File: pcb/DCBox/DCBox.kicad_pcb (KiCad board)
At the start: 2 copper layers, 60 x 50 mm, 7 parts, among them J1 DC-IN, J2 Out-1, J3 Out-2, J4 Out-3

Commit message: 1. 完善布局
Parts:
- added C1: NC, lc_lib:0603_R, F.Cu at (163.9, 64.1)
- added C10: 1uF, lc_lib:0603_R, F.Cu at (150.3, 63.9)
- added C11: NC, lc_lib:0603_R, F.Cu at (169.8, 54.7)
- added C12: NC, lc_lib:0603_R, F.Cu at (173.3, 49.2)
- added C13: NC, lc_lib:0603_R, F.Cu at (177.6, 46.4)
- added C14: 22uF, lc_lib:1206_R, F.Cu at (164.0, 46.8)
- added C15: 100nF, lc_lib:0603_R, F.Cu at (155.7, 69.9)
- added C16: 100nF, lc_lib:0603_R, F.Cu at (155.4, 61.5)
- added C17: 22uF, lc_lib:1206_R, F.Cu at (157.8, 52.6)
- added C18: 100nF, lc_lib:0603_R, F.Cu at (159.6, 61.5)
- added C19: 22uF, lc_lib:1206_R, F.Cu at (156.2, 58.3)
- added C2: NC, lc_lib:0603_R, F.Cu at (155.7, 67.1)
- added C20: 100nF, lc_lib:0603_R, F.Cu at (163.9, 61.3)
- added C21: NC, lc_lib:0603_R, F.Cu at (143.3, 79.7)
- added C22: NC, lc_lib:0603_R, F.Cu at (169.1, 49.2)
- added C3: NC, lc_lib:0603_R, F.Cu at (155.7, 72.6)
- added C4: 4.7uF, lc_lib:0603_R, F.Cu at (151.5, 72.3)
- added C5: 100nF, lc_lib:0603_R, F.Cu at (139.1, 80.4)
- added C6: 4.7uF, lc_lib:0603_R, F.Cu at (142.9, 74.2)
- added C7: 100nF, lc_lib:0603_R, F.Cu at (151.5, 69.5)
- added C8: 2.2uF, lc_lib:0603_R, F.Cu at (169.1, 46.4)
- added C9: 1uF, lc_lib:0603_R, F.Cu at (134.8, 80.4)
- added D1: LED, lc_lib:0603_LED_N1, F.Cu at (151.4, 49.4)
- added D2: LED, lc_lib:0603_LED_N1, F.Cu at (151.4, 46.5)
- added D3: LED, lc_lib:0603_LED_N1, F.Cu at (157.6, 49.4)
- added D4: LED, lc_lib:0603_LED_N1, F.Cu at (151.4, 55.1)
- added D5: LED, lc_lib:0603_LED_N1, F.Cu at (151.4, 52.3)
- added D6: LED, lc_lib:0603_LED_N1, F.Cu at (144.8, 64.0)
- added D7: LED, lc_lib:0603_LED_N1, F.Cu at (157.6, 46.5)
- added J5: Out-4, jld:DC005, F.Cu at (162.3, 151.1)
- added J6: USB_A, Connector_USB:USB_A_Wuerth_614004134726_Horizontal, F.Cu at (158.7, 117.7)
- added J7: USB_A, Connector_USB:USB_A_Wuerth_614004134726_Horizontal, F.Cu at (158.7, 128.7)
- added J8: Conn_01x04, Connector_PinHeader_2.54mm:PinHeader_1x04_P2.54mm_Vertical, F.Cu at (146.3, 47.3)
- added R10: 560k, lc_lib:0603_R, F.Cu at (147.2, 71.4)
- added R11: 1R/2W/%1, lc_lib:2512_R, B.Cu at (162.3, 147.4)
- added R12: 1k, lc_lib:0603_R, F.Cu at (165.5, 57.5)
- added R13: 20k, lc_lib:0603_R, F.Cu at (169.8, 57.5)
- added R14: 10k, lc_lib:0603_R, F.Cu at (134.8, 77.7)
- added R15: 1R/2W/%1, lc_lib:2512_R, B.Cu at (166.9, 117.7)
- added R16: 1R/2W/%1, lc_lib:2512_R, B.Cu at (166.7, 128.5)
- added R17: 15k, lc_lib:0603_R, F.Cu at (154.6, 64.3)
- added R18: 20k, lc_lib:0603_R, F.Cu at (168.2, 60.3)
- added R19: 4.7k, lc_lib:0603_R, F.Cu at (147.6, 79.7)
- added R20: 4.7k, lc_lib:0603_R, F.Cu at (139.1, 77.7)
- added R21: 1k, lc_lib:0603_R, F.Cu at (161.3, 58.5)
- added R22: 1k, lc_lib:0603_R, F.Cu at (147.6, 76.9)
- added R23: 1k, lc_lib:0603_R, F.Cu at (168.4, 52.0)
- added R24: 1k, lc_lib:0603_R, F.Cu at (143.3, 76.9)
- added R25: 1k, lc_lib:0603_R, F.Cu at (174.1, 54.7)
- added R26: 1k, lc_lib:0603_R, F.Cu at (149.2, 66.8)
- added R27: 10k, lc_lib:0603_R, F.Cu at (165.5, 54.7)
- added R28: 1k, lc_lib:0603_R, F.Cu at (151.9, 75.4)
- added R29: 1k, lc_lib:0603_R, F.Cu at (158.9, 64.3)
- added R30: 1.5k, lc_lib:0603_R, F.Cu at (172.7, 52.0)
- added R4: 1k, lc_lib:0603_R, F.Cu at (147.2, 74.2)
- added R5: 1k, lc_lib:0603_R, F.Cu at (160.0, 67.1)
- added R6: 1k, lc_lib:0603_R, F.Cu at (173.3, 46.4)
- added R7: 4.7k, lc_lib:0603_R, F.Cu at (177.6, 49.2)
- added R8: 4.7k, lc_lib:0603_R, F.Cu at (142.9, 71.4)
- added R9: 4.7k, lc_lib:0603_R, F.Cu at (161.3, 55.8)
- added SW1: SW_Push, jld:Button_SW_THT_6.2x6.2, F.Cu at (105.4, 108.0)
- added U1: MT2492, lc_lib:SOT-23-6, F.Cu at (158.8, 88.8)
- added U2: 662K, lc_lib:SOT-23-3L, F.Cu at (163.7, 50.8)
- added U3: STC8H1K08_TSSOP20, lc_lib:TSSOP-20, F.Cu at (123.5, 129.5)
- J1: value DC-IN -> Out-1
- J2: value Out-1 -> Out-2
- J3: value Out-2 -> Out-3
- J4: value Out-3 -> DC-IN
- R1, R2, R3: value 1R -> 1R/2W/%1; moved to B.Cu
- moved J4 58.2 mm to (108.5, 151.1), turned to 0 degrees
- moved R1 47.7 mm to (126.2, 147.7)
- moved J1 47.0 mm to (126.0, 151.1), turned to 0 degrees
- moved J3 43.9 mm to (150.0, 151.1), turned to 0 degrees
- moved J2 38.9 mm to (138.2, 151.1), turned to 0 degrees
- moved R3 31.0 mm to (150.2, 147.4), turned to 180 degrees
- moved R2 19.0 mm to (138.3, 147.5), turned to 180 degrees
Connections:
- J1 pad 2: GND -> Net-(J1-Pad2)
- J4 pad 2: Net-(J4-Pad2) -> GND
- R1 pad 2: Net-(J2-Pad2) -> Net-(J1-Pad2)
- R2 pad 2: Net-(J3-Pad2) -> Net-(J2-Pad2)
- R3 pad 2: Net-(J4-Pad2) -> Net-(J3-Pad2)
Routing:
- net +12V: track 68.5 -> 0.00 mm
- removed copper zone on B.Cu, net GND
- removed copper zone on F.Cu, net GND
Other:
- board size 60 x 50 mm -> 70 x 50 mm

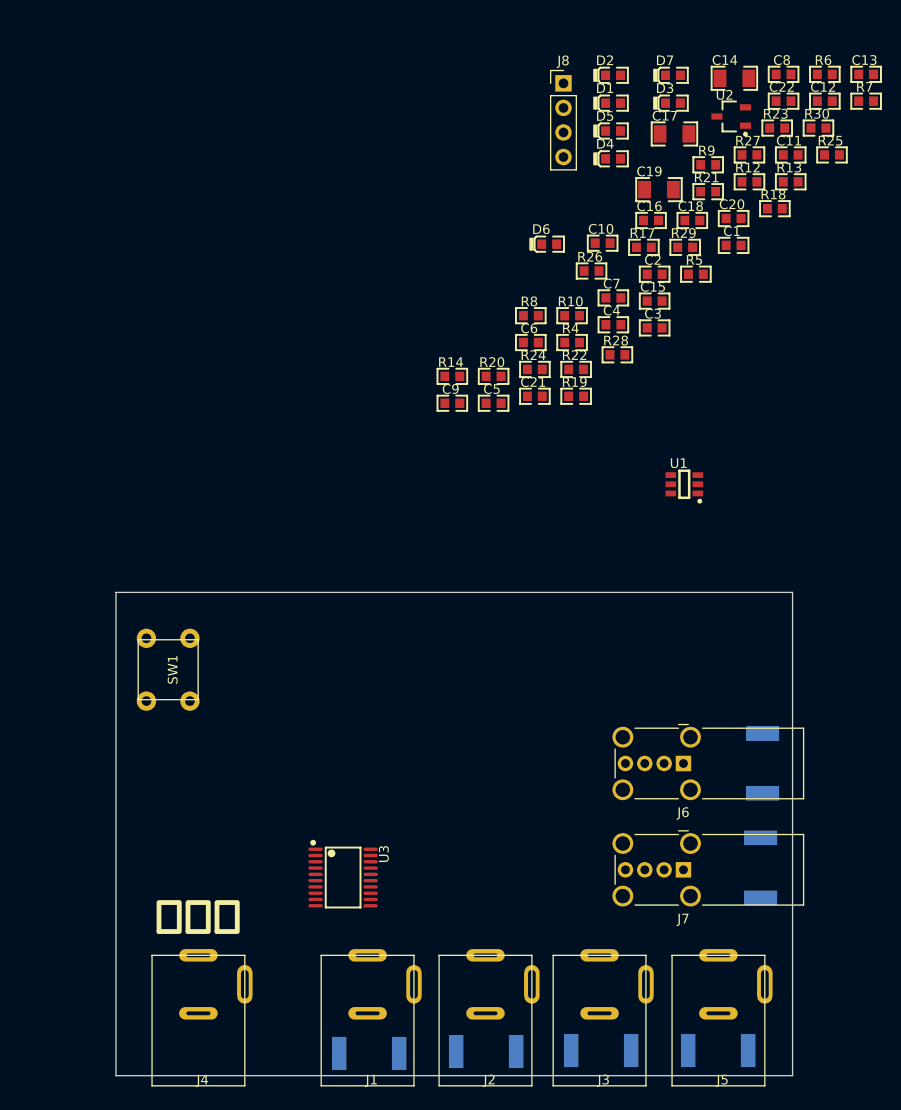
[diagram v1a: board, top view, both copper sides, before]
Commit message: 1. 进线DC增加可恢复保险丝 2. 布局完善
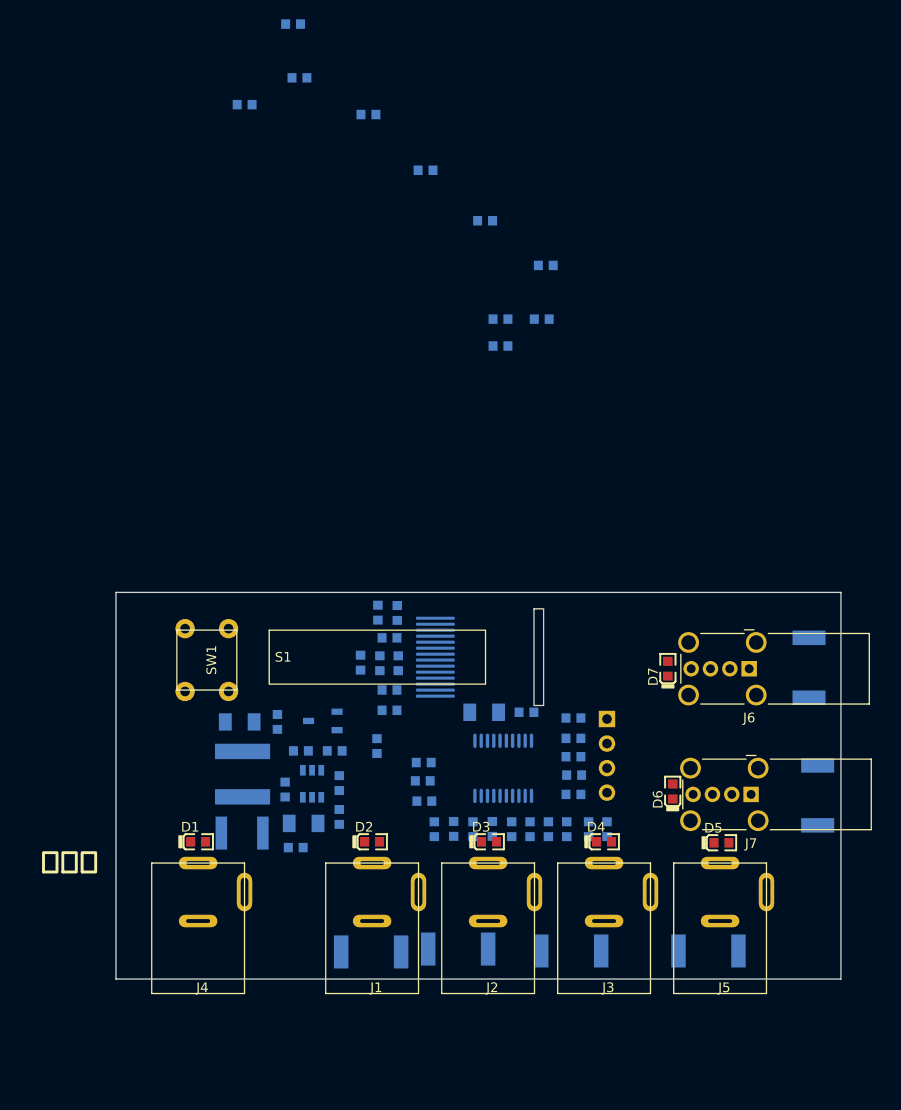
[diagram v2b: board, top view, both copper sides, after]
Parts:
- added L1: 10uH, Inductor_SMD:L_Bourns-SRN6028, B.Cu at (113.1, 118.8)
- added R31: 1k, lc_lib:0603_R, B.Cu at (147.3, 113.0)
- added R32: 1k, lc_lib:0603_R, B.Cu at (150.8, 124.5)
- added S1: OLED_091, jld:ZJY09_Screen, F.Cu at (127.0, 106.7)
- added TH1: 16V/2A, lc_lib:1812_R, B.Cu at (113.0, 124.9)
- C1, C10, C11, C12, C13, C14, C15, C16, C17, C18, C19, C2, C20, C21, C22, C3, C4, C5, C6, C7, C8, C9, J8, R10, R12, R13, R14, R17, R18, R19, R20, R21, R22, R23, R24, R25, R26, R27, R28, R29, R30, R4, R5, R6, R7, R8, R9, U1, U2, U3: moved to B.Cu
- moved C14 89.0 mm to (119.4, 123.9), turned to 180 degrees
- moved D1 87.6 mm to (108.5, 125.8)
- moved C13 84.7 mm to (144.7, 124.5), turned to -90 degrees
- moved R6 83.8 mm to (142.8, 124.5), turned to 90 degrees
- moved D2 83.1 mm to (126.5, 125.8)
- moved R13 80.6 mm to (123.1, 123.2), turned to 90 degrees
- moved C12 79.2 mm to (148.9, 124.5), turned to -90 degrees
- moved D3 78.8 mm to (138.6, 125.8)
- moved R7 78.2 mm to (125.3, 107.3), turned to 90 degrees
- moved C17 75.7 mm to (112.8, 113.4), turned to 180 degrees
- moved U2 75.5 mm to (121.4, 113.3)
- moved C22 74.9 mm to (147.3, 120.9)
- moved D5 74.5 mm to (162.6, 125.9)
- moved R18 72.3 mm to (122.6, 116.4)
- moved R30 71.6 mm to (147.4, 118.9)
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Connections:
- C11 pad 2: GND -> Net-(C11-Pad2)
- C12 pad 2: GND -> Net-(J7-Pad4)
- J4 pad 1: +12V -> Net-(J4-Pad1)
- J6 pad 4: /ADC_Current_USB1 -> Net-(C11-Pad2)
- J6 pad 5: /ADC_Current_USB1 -> Net-(C11-Pad2)
- J7 pad 4: /ADC_Current_USB2 -> Net-(J7-Pad4)
- J7 pad 5: /ADC_Current_USB2 -> Net-(J7-Pad4)
- R15 pad 1: /ADC_Current_USB1 -> Net-(C11-Pad2)
- R16 pad 1: /ADC_Current_USB2 -> Net-(J7-Pad4)
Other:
- board size 70 x 50 mm -> 75 x 40 mm

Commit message: 1. 布局基本完成
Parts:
- added H1: MountingHole, MountingHole:MountingHole_2.2mm_M2, F.Cu at (103.0, 103.0)
- added H2: MountingHole, MountingHole:MountingHole_2.2mm_M2, F.Cu at (103.0, 137.0)
- added H3: MountingHole, MountingHole:MountingHole_2.2mm_M2, F.Cu at (172.0, 137.0)
- added H4: MountingHole, MountingHole:MountingHole_2.2mm_M2, F.Cu at (172.0, 103.0)
- moved R25 70.0 mm to (146.8, 111.0), turned to 0 degrees
- moved R23 69.3 mm to (125.1, 115.8)
- moved C8 63.0 mm to (125.1, 103.8), turned to 0 degrees
- moved C16 55.9 mm to (125.1, 111.8), turned to 0 degrees
- moved R9 55.2 mm to (125.1, 105.8), turned to 0 degrees
- moved R26 48.2 mm to (146.8, 109.0), turned to 0 degrees
- moved R24 46.7 mm to (128.6, 115.8)
- moved R22 43.5 mm to (128.6, 113.8)
- moved R8 42.7 mm to (128.6, 105.8), turned to 0 degrees
- moved R19 41.3 mm to (133.6, 115.3)
- moved TH1 7.98 mm to (120.4, 128.0)
- moved R20 7.53 mm to (111.5, 123.8), turned to 180 degrees
- moved R15 4.24 mm to (169.3, 111.3), turned to 90 degrees
- moved C4 4.01 mm to (125.1, 101.8), turned to 0 degrees
- moved U2 3.90 mm to (117.5, 113.2)
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- renumbered C11 to R29
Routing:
- net +12V: track 0.00 -> 51.2 mm
- net +5V: track 0.00 -> 12.1 mm
- net Net-(J4-Pad1): track 0.00 -> 6.78 mm
- net Net-(C15-Pad2): track 0.00 -> 6.30 mm
- net Net-(R13-Pad2): track 0.00 -> 4.31 mm
- net Net-(R17-Pad2): track 0.00 -> 4.21 mm
- net Net-(C15-Pad1): track 0.00 -> 2.40 mm
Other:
- board text added: "进线"
- board text removed: "总进线"

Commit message: 1. 布线
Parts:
- moved R20 0.59 mm to (112.1, 123.7)
- moved C19 0.20 mm to (138.0, 112.5)
- moved U3 0.20 mm to (140.3, 118.0)
- moved C20 0.20 mm to (142.7, 112.9)
- turned D1 to 180 degrees
- turned D2 to 180 degrees
- turned R21 to 180 degrees
- turned R22 to 0 degrees
- turned R24 to 0 degrees
- turned SW1 to -90 degrees
- renumbered R29 to C11
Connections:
- C11 pad 2: Net-(C11-Pad2) -> GND
- C12 pad 2: Net-(C12-Pad2) -> GND
- J6 pad 4: Net-(C11-Pad2) -> Net-(J6-Pad4)
- J6 pad 5: Net-(C11-Pad2) -> Net-(J6-Pad4)
- J7 pad 4: Net-(C12-Pad2) -> Net-(J7-Pad4)
- J7 pad 5: Net-(C12-Pad2) -> Net-(J7-Pad4)
- R15 pad 1: Net-(C11-Pad2) -> Net-(J6-Pad4)
- R16 pad 1: Net-(C12-Pad2) -> Net-(J7-Pad4)
- R31 pad 2: Net-(C11-Pad2) -> Net-(J6-Pad4)
- R32 pad 2: Net-(C12-Pad2) -> Net-(J7-Pad4)
- U3 pad 1: /SDA -> /SCL
- U3 pad 2: /SCL -> /SDA
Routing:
- net +3V3: track 0.00 -> 65.2 mm
- net /Key_Config: track 0.00 -> 27.1 mm
- net /SDA: track 0.00 -> 22.7 mm
- net Net-(J5-Pad2): track 0.00 -> 20.8 mm
- net +12V: track 51.2 -> 72.0 mm
- net /SCL: track 0.00 -> 18.2 mm
- net /ADC_Voltage_5V: track 0.00 -> 14.7 mm
- net Net-(D2-Pad2): track 0.00 -> 14.6 mm, vias 0 -> 1
- net Net-(J3-Pad2): track 0.00 -> 13.8 mm
- net Net-(J6-Pad4): track 0.00 -> 10.9 mm
- net /ADC_Current_USB2: track 0.00 -> 10.6 mm
- net /ADC_Current_USB1: track 0.00 -> 10.6 mm
- net Net-(J2-Pad2): track 0.00 -> 10.1 mm
- net Net-(R7-Pad2): track 0.00 -> 9.56 mm
- net /ADC_Current_DC4: track 0.00 -> 8.03 mm
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
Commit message: 1. PCB基本完成
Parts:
- moved R22 4.03 mm to (125.1, 115.8), turned to 180 degrees
- moved R23 3.50 mm to (128.6, 115.8), turned to 0 degrees
- moved R24 2.00 mm to (128.6, 113.8)
- moved R15 0.80 mm to (169.3, 110.5)
- turned D3 to 180 degrees
- turned D4 to 180 degrees
- turned D5 to 180 degrees
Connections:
- U3 pad 18: /LED_USB2 -> /LED_DC1
- U3 pad 3: /LED_DC1 -> /LED_DC2
- U3 pad 4: /LED_DC2 -> /LED_DC3
- U3 pad 5: /LED_DC3 -> /LED_DC4
- U3 pad 6: /LED_DC4 -> /LED_USB1
- U3 pad 7: /LED_USB1 -> /LED_USB2
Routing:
- net +5V: track 19.0 -> 79.2 mm, vias 0 -> 1
- net +3V3: track 65.2 -> 124.1 mm, vias 0 -> 2
- net /Key_Config: track 27.1 -> 67.3 mm, vias 0 -> 2
- net Net-(D5-Pad2): track 0.00 -> 38.9 mm, vias 0 -> 1
- net GND: track 0.00 -> 35.8 mm, vias 0 -> 32
- net /LED_DC4: track 0.00 -> 30.1 mm, vias 0 -> 1
- net Net-(D4-Pad2): track 0.00 -> 27.3 mm, vias 0 -> 1
- net Net-(J6-Pad4): track 10.9 -> 35.1 mm
- net Net-(J7-Pad4): track 7.70 -> 31.4 mm
- net Net-(D3-Pad2): track 0.00 -> 23.0 mm, vias 0 -> 1
- net /LED_DC3: track 0.00 -> 20.2 mm, vias 0 -> 1
- net /LED_USB2: track 0.00 -> 19.8 mm, vias 0 -> 1
- net /LED_USB1: track 0.00 -> 18.7 mm, vias 0 -> 1
- net Net-(D6-Pad2): track 0.00 -> 16.2 mm, vias 0 -> 1
- net /LED_DC1: track 0.00 -> 14.8 mm, vias 0 -> 1
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- added copper zone on B.Cu, net GND
- added copper zone on F.Cu, net GND
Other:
- outline, holes or cut-outs redrawn
- board text added: "1"
- board text added: "12V-IN"
- board text added: "2"
- board text added: "3"
- board text added: "4"
- board text added: "FUSE"
- board text added: "USB-5"
- board text added: "USB-6"
- board text added: "V1.0"
- board text added: "分线盒12V/5V"
- board text removed: "进线"
